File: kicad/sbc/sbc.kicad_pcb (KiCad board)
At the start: 4 copper layers, 238.1 x 142.2 mm, 155 parts, among them CON1 BARREL_JACK, IC1 ATMEGA8-P, J1 USB, J2 DB9, J3 Audio, J4 S-VIDEO, J5 RGB, P1 USERPORT, P2 CONN_01X03, P3 ISP, P4 PS/2 Keyboard, SW1 SW_PUSH, U1 W65C02, U10 LM555N, U11 W65C22NxPL, U12 74HCT245, U13 74HCT245, U14 7407, U15 Micro_SD_Card_Det1, U16 YM3812, U17 74LS139, U18 V9958, U19 DRAM_64KX4, U2 CHUCK, U20 DRAM_64KX4, U21 DRAM_64KX4, U22 DRAM_64KX4, U23 DRAM_64KX4, U24 DRAM_64KX4, U25 Y3014B, U26 LM324, U27 cxa2075M, U28 7400, U29 74LS244, U3 AS6C4008, U30 DS1306, U4 28C256, U5 74LS06, U6 16550, U7 74125, U8 MAX232, U9 LP2950, X1 OSC, X2 OSC, X3 OSC, X4 CRYSTAL_SMD, Y1 21,443Mhz

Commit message: removed U17
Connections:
- U2 pad 11: unconnected-(U2-P11-Pad11) -> /~{W}
- U2 pad 25: unconnected-(U2-P25-Pad25) -> /~{CSW_VDP}
- U2 pad 26: unconnected-(U2-P26-Pad26) -> /~{R}
- U2 pad 47: /~{CS_VDP} -> /~{CSR_VDP}
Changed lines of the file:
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@@
   (net 60 "/CLKIN")
   (net 61 "unconnected-(U2-I{slash}O{slash}GCK2-Pad10)")
-  (net 62 "unconnected-(U2-P11-Pad11)")
+  (net 62 "/~{W}")
   (net 63 "unconnected-(U2-I{slash}O{slash}GCK3-Pad12)")
   (net 64 "unconnected-(U2-P15-Pad15)")
@@
   (net 69 "unconnected-(U2-P23-Pad23)")
   (net 70 "unconnected-(U2-P24-Pad24)")
-  (net 71 "unconnected-(U2-P25-Pad25)")
-  (net 72 "unconnected-(U2-P26-Pad26)")
+  (net 71 "/~{CSW_VDP}")
+  (net 72 "/~{R}")
   (net 73 "unconnected-(U2-P31-Pad31)")
   (net 74 "unconnected-(U2-P32-Pad32)")
@@
   (net 309 "unconnected-(U30-1HZ-Pad7)")
   (net 310 "unconnected-(U30-32KHZ-Pad15)")
+  (net 311 "/~{CSR_VDP}")
   (footprint "Package_LCC:PLCC-44_THT-Socket" (layer "F.Cu")
     (at 151.765 182.225)
@@
       (net 61 "unconnected-(U2-I{slash}O{slash}GCK2-Pad10)") (pinfunction "I/O/GCK2") (pintype "bidirectional"))
     (pad "11" thru_hole circle (at -12.7 0 180) (size 1.4224 1.4224) (drill 0.8) (layers "*.Cu" "*.Mask")
-      (net 62 "unconnected-(U2-P11-Pad11)") (pinfunction "P11") (pintype "bidirectional"))
+      (net 62 "/~{W}") (pinfunction "P11") (pintype "bidirectional"))
     (pad "12" thru_hole circle (at -15.24 2.54 180) (size 1.4224 1.4224) (drill 0.8) (layers "*.Cu" "*.Mask")
       (net 63 "unconnected-(U2-I{slash}O{slash}GCK3-Pad12)") (pinfunction "I/O/GCK3") (pintype "bidirectional"))
@@
       (net 70 "unconnected-(U2-P24-Pad24)") (pinfunction "P24") (pintype "bidirectional"))
     (pad "25" thru_hole circle (at -12.7 17.78 180) (size 1.4224 1.4224) (drill 0.8) (layers "*.Cu" "*.Mask")
-      (net 71 "unconnected-(U2-P25-Pad25)") (pinfunction "P25") (pintype "bidirectional"))
+      (net 71 "/~{CSW_VDP}") (pinfunction "P25") (pintype "bidirectional"))
     (pad "26" thru_hole circle (at -15.24 20.32 180) (size 1.4224 1.4224) (drill 0.8) (layers "*.Cu" "*.Mask")
-      (net 72 "unconnected-(U2-P26-Pad26)") (pinfunction "P26") (pintype "bidirectional"))
+      (net 72 "/~{R}") (pinfunction "P26") (pintype "bidirectional"))
     (pad "27" thru_hole circle (at -12.7 20.32 180) (size 1.4224 1.4224) (drill 0.8) (layers "*.Cu" "*.Mask")
       (net 1 "GND") (pinfunction "GND") (pintype "power_in"))
@@
       (net 216 "unconnected-(U2-P46-Pad46)") (pinfunction "P46") (pintype "bidirectional"))
     (pad "47" thru_hole circle (at 5.08 30.48 180) (size 1.4224 1.4224) (drill 0.8) (layers "*.Cu" "*.Mask")
-      (net 143 "/~{CS_VDP}") (pinfunction "P47") (pintype "bidirectional"))
+      (net 311 "/~{CSR_VDP}") (pinfunction "P47") (pintype "bidirectional"))
     (pad "48" thru_hole circle (at 5.08 27.94 180) (size 1.4224 1.4224) (drill 0.8) (layers "*.Cu" "*.Mask")
       (net 106 "/~{CS_UART}") (pinfunction "P48") (pintype "bidirectional"))

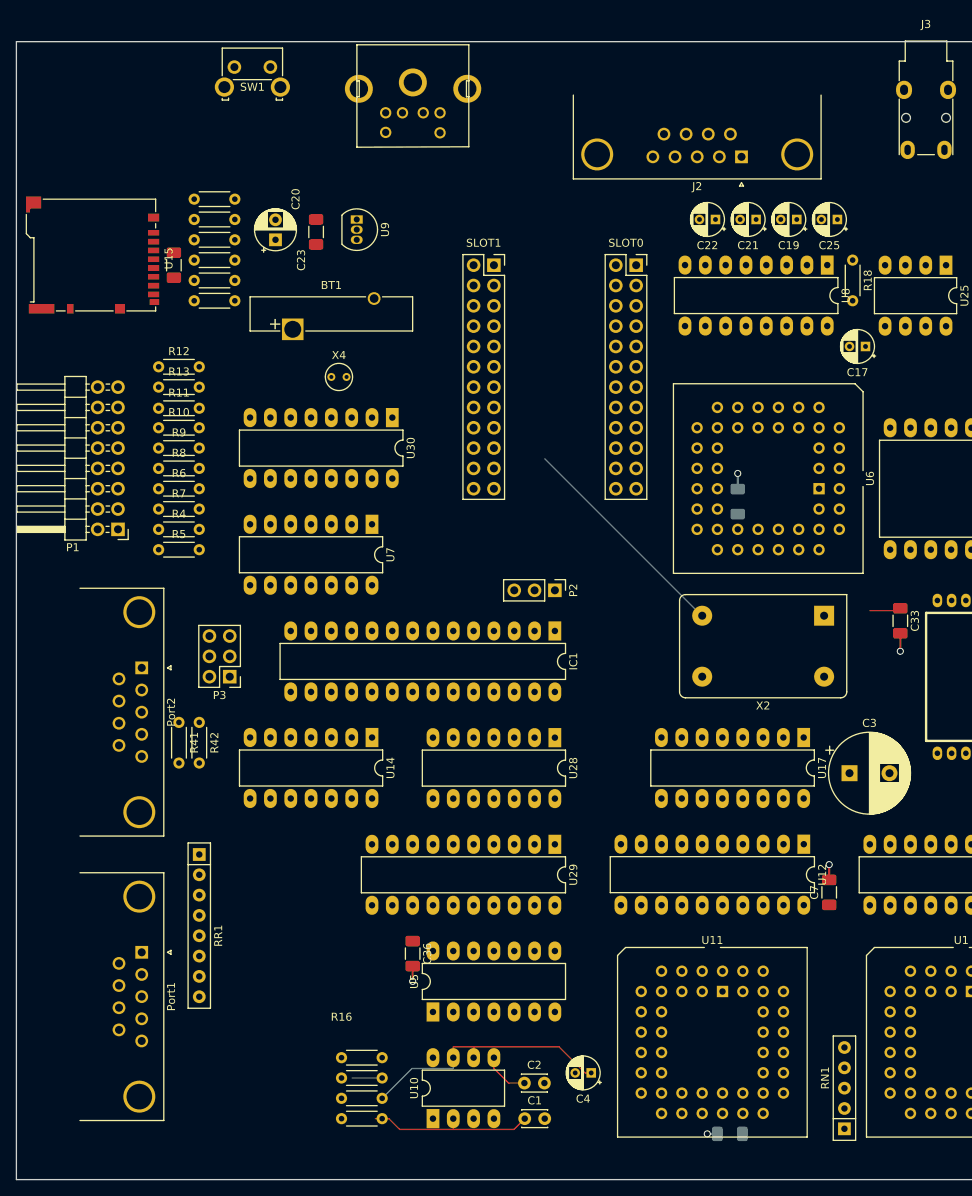
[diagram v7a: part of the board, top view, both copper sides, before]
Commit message: io area placement
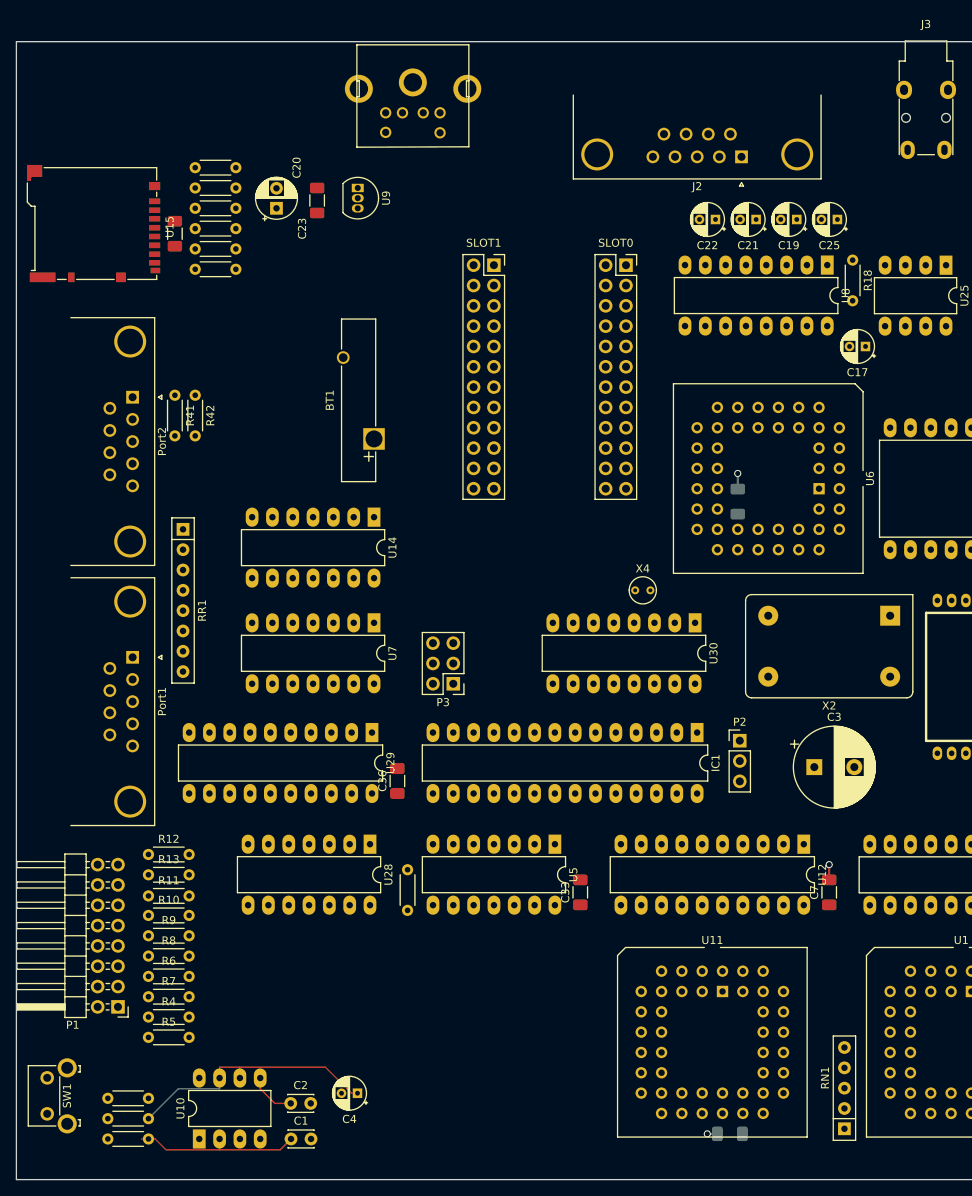
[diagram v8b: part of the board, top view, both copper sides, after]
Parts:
- removed U17: 74LS139, Package_DIP:DIP-16_W7.62mm_LongPads
- moved SW1 132.9 mm to (67.3, 197.5), turned to 90 degrees
- moved R11 61.0 mm to (80.0, 170.3)
- moved R5 61.0 mm to (80.0, 188.0)
- moved R6 61.0 mm to (80.0, 180.3)
- moved R8 61.0 mm to (80.0, 177.8)
- moved R10 61.0 mm to (80.0, 172.7)
- moved R12 61.0 mm to (80.0, 165.1)
- moved R4 61.0 mm to (80.0, 185.4)
- moved R7 61.0 mm to (80.0, 182.9)
- moved R9 61.0 mm to (80.0, 175.3)
- moved R13 61.0 mm to (80.0, 167.6)
- moved P1 59.7 mm to (76.2, 184.2)
- moved C33 52.5 mm to (134.0, 169.8), turned to 90 degrees
- moved X4 46.4 mm to (140.8, 132.1)
- moved U30 45.7 mm to (148.3, 136.1)
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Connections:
- U16 pad 5: /Video_Audio//CSW_OPL3 -> /~{W}
- U16 pad 6: /Video_Audio//CSR_OPL3 -> /~{R}
- U18 pad 30: Net-(U17B-O0) -> /~{CSW_VDP}
- U18 pad 31: Net-(U17B-O1) -> /~{CSR_VDP}
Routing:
- net /BUF_D0: track 26.5 -> 0.00 mm
- net GND: track 61.1 -> 56.9 mm, vias 22 -> 20
- net VCC: track 36.9 -> 32.9 mm
- net /~{RESET}: track 3.74 -> 0.00 mm
